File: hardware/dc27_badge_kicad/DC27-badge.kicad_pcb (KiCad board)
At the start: 4 copper layers, 79.1 x 184.5 mm, 129 parts, among them J101 Conn_ARM_JTAG_SWD_10, J102 ShittyAddOnL, J103 ShittyAddOnR, J104 Conn_02x20_Odd_Even, J501 SPK LEFT, J502 SPK_RIGHT, J601 USB_MICRO_RIGHT, SW101 UP, SW102 DN, SW103 LEFT, SW104 RIGHT, SW105 A, SW106 B, SW107 ENTER, SW108 RESET, SW401 POWER ON, U100 BMD-340-A-R-DC27-peripheral-c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, U301 IS31FL3216A, U401 MCP73831-2-OT, U402 LM1117-3.3, U403 MAX17055, U501 CS4344-CZZ, U502 LM4880, U601 CP2102N-A01-GQFN28, U602 TPD3E001DRLR, Y101 32.768Khz XTAL

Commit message: check in all of the gerbers and artwork
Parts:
- C506: footprint Capacitor_SMD:C_0603_1608Metric -> Capacitor_SMD:CP_Elec_5x5.3; moved to F.Cu
- U403: value MAX17055 -> MAX17055-10-TDFN-EP; footprint SON50P300X300X80-11N:SON50P300X300X80-11N -> tdfn-10-ep-2.00x2:tdfn-10-ep-2.00x2.50
- moved C506 23.4 mm to (118.3, 75.7), turned to 270 degrees
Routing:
- net Net-(C506-Pad1): track 2.39 -> 24.4 mm, vias 0 -> 1
- net Net-(C506-Pad2): track 10.0 -> 30.4 mm, vias 0 -> 1
- net I2C_SCK: track 332.5 -> 346.9 mm
- net Net-(C510-Pad1): track 62.1 -> 58.2 mm
- net BATT_CSN: track 453.5 -> 457.2 mm
- net Net-(C505-Pad1): track 48.4 -> 46.4 mm
- net BATT_CSP: track 15.6 -> 16.2 mm
- net I2S_SDOUT: track 88.8 -> 89.4 mm, vias 4 -> 3

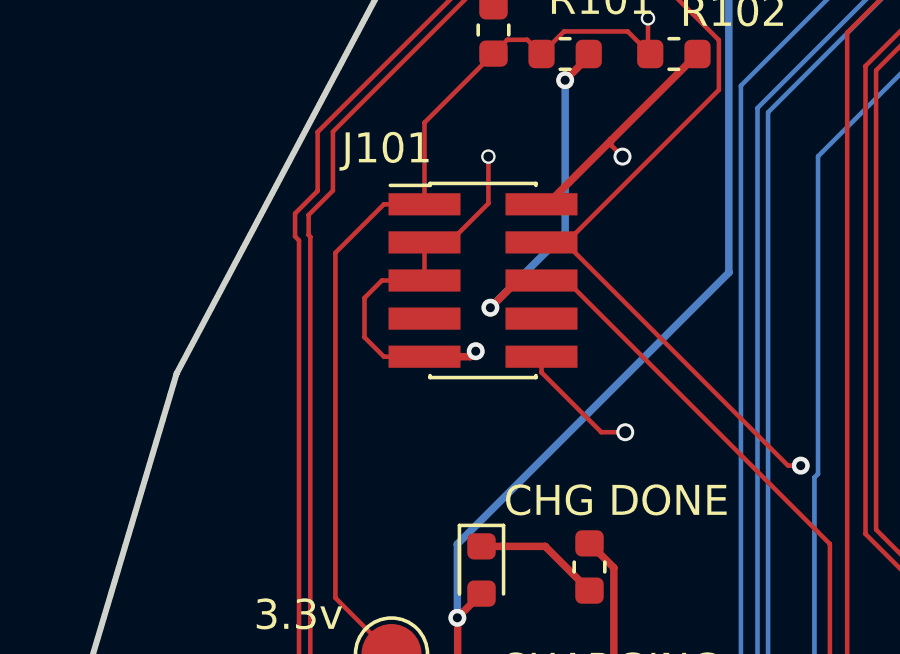
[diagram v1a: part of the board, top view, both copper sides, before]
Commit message: Closes issues #1, #2, #3 (see github)
  - #1 Removes copper fill under bmd340
  - #2 Add ON label
  - #3 Add pin 1 indicator and label for jtag
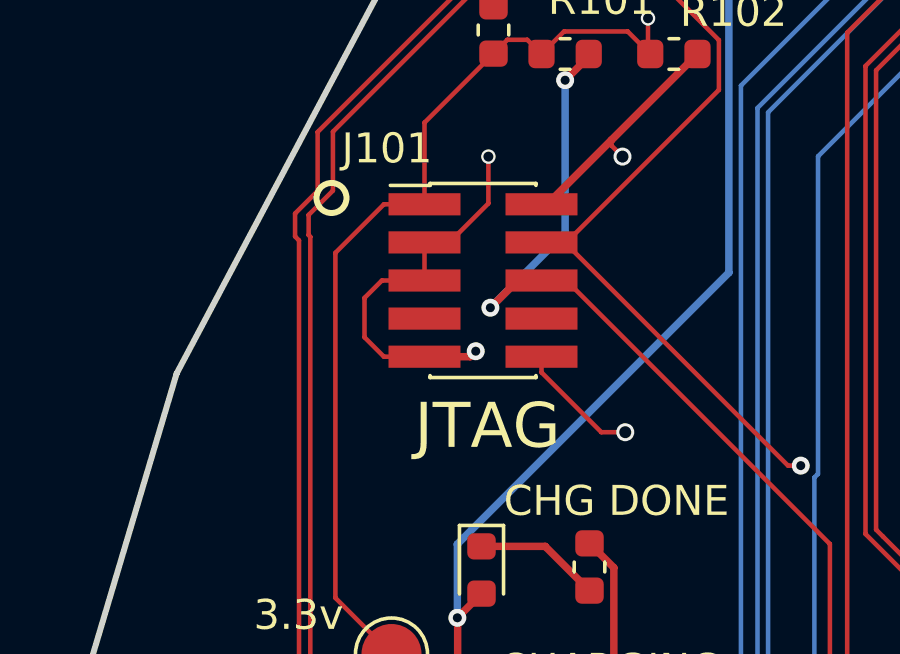
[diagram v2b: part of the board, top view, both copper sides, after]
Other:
- board text added: "JTAG"
- board text added: "ON"
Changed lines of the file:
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@@
-(kicad_pcb (version 20171130) (host pcbnew "(5.0.1-3-g963ef8bb5)")
+(kicad_pcb (version 20171130) (host pcbnew "(5.0.2-5)-5")
   (general
     (thickness 1.6)
-    (drawings 185)
+    (drawings 188)
     (tracks 2446)
     (zones 0)
@@
   )
   (setup
-    (last_trace_width 0.1524)
+    (last_trace_width 0.25)
     (user_trace_width 0.1524)
     (user_trace_width 0.254)
@@
       (net 156 BATT_CSN))
   )
+  (gr_text JTAG (at 81.6 107.6) (layer F.SilkS)
+    (effects (font (size 1.5 1.5) (thickness 0.3)))
+  )
+  (gr_circle (center 76.4 100) (end 76.7 100.4) (layer F.SilkS) (width 0.2))
+  (gr_text ON (at 71.2 115) (layer B.SilkS)
+    (effects (font (size 1.5 1.5) (thickness 0.3)) (justify mirror))
+  )
   (gr_text SDT_SPI_SCLK (at 119.2 140.2) (layer F.SilkS)
     (effects (font (size 1 1) (thickness 0.2)))
@@
     (connect_pads (clearance 0.508))
     (min_thickness 0.254)
-    (keepout (tracks not_allowed) (vias not_allowed) (copperpour allowed))
+    (keepout (tracks not_allowed) (vias not_allowed) (copperpour not_allowed))
     (fill (mode segment) (arc_segments 16) (thermal_gap 0.508) (thermal_bridge_width 0.508))
     (polygon

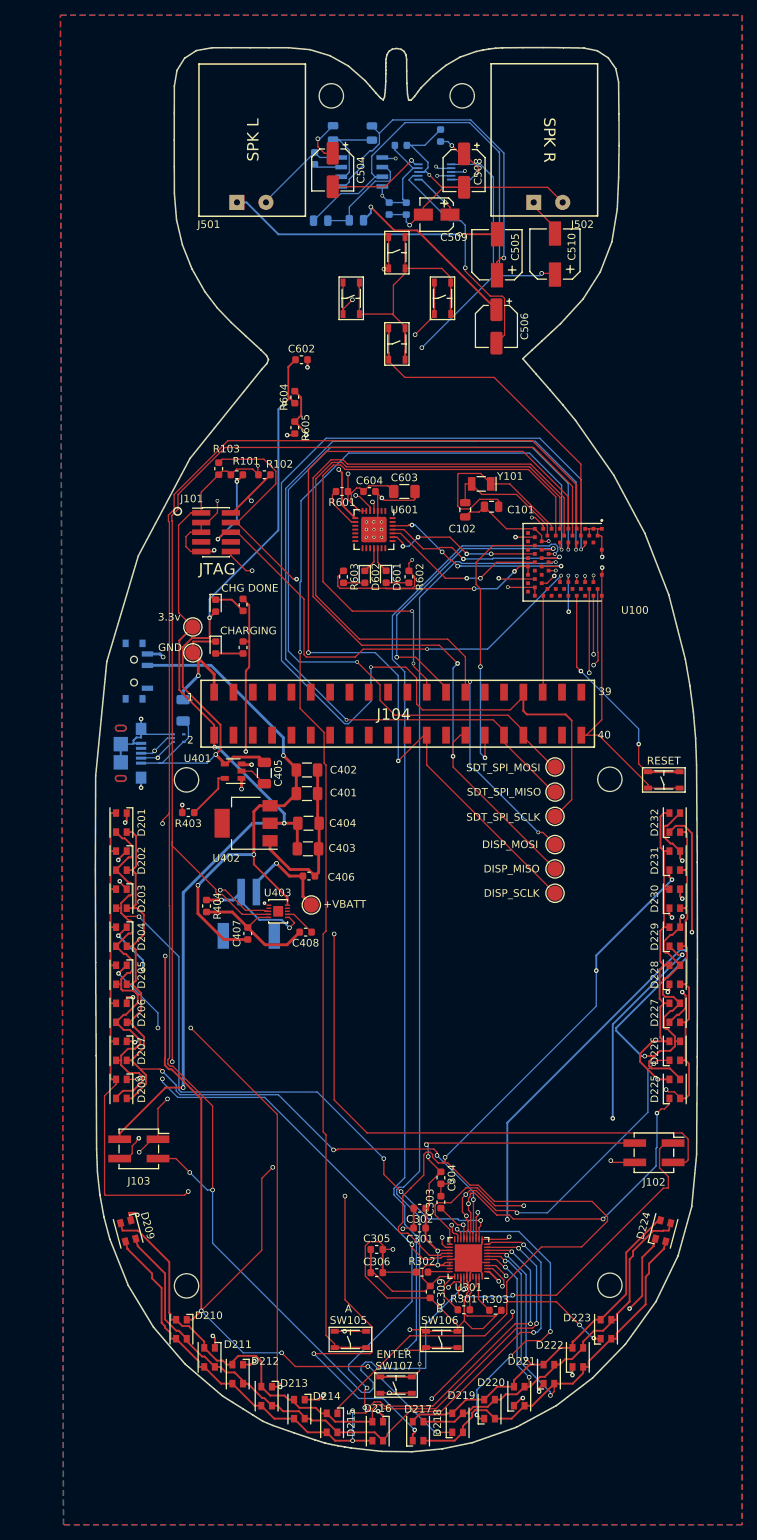
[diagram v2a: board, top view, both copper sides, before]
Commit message: add AST-01078 3d model and kicad footprint, check in current budget, update charging circut to MCP73833 instead of MCP73831:
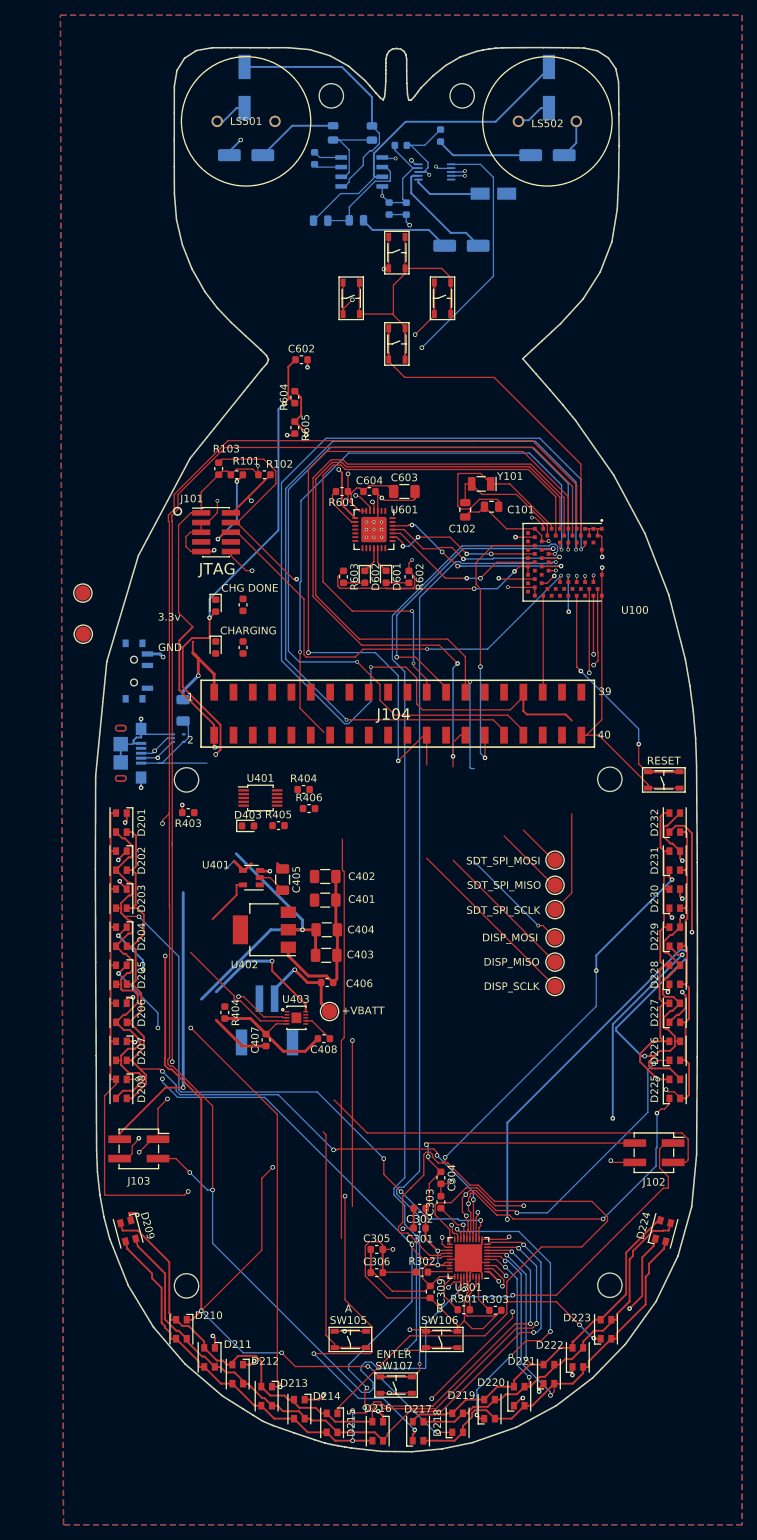
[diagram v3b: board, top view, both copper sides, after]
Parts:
- removed J501: SPK LEFT, Connector_Wire:SolderWirePad_1x02_P3.81mm_Drill0.8mm
- removed J502: SPK_RIGHT, Connector_Wire:SolderWirePad_1x02_P3.81mm_Drill0.8mm
- added D403: PWR GOOD, Diode_SMD:D_0603_1608Metric, F.Cu at (85.7, 141.3)
- added LS501: Speaker, lib_fp:AST-01708-MRR, F.Cu at (85.4, 48.8)
- added LS502: Speaker, lib_fp:AST-01708-MRR, F.Cu at (125.0, 48.8)
- added R404: 2.0k, Resistor_SMD:R_0603_1608Metric, F.Cu at (93.0, 136.6)
- added R405: 1K, Resistor_SMD:R_0603_1608Metric, F.Cu at (89.7, 141.3)
- added R406: 10K, Resistor_SMD:R_0603_1608Metric, F.Cu at (93.7, 139.1)
- added U401: MCP73833, Package_SO:MSOP-10_3x3mm_P0.5mm, F.Cu at (87.3, 137.7)
- C406: value 1uF -> 10uF
- C504, C505, C506, C508, C509, C510: moved to B.Cu
- D401: value CHG -> CHARGED
- D402: value DONE -> CHARGING (ORANGE)
- moved C505 39.8 mm to (85.2, 44.3)
- moved C510 21.9 mm to (125.2, 44.3)
- moved TP402 15.1 mm to (64.0, 110.8)
- moved TP403 14.6 mm to (64.0, 116.2)
- moved BT401 14.2 mm to (88.2, 166.9)
- moved C403 14.2 mm to (95.9, 158.4)
- moved C404 14.2 mm to (96.0, 155.0)
- moved C405 14.2 mm to (90.2, 148.4)
- moved C406 14.2 mm to (96.1, 161.9)
- moved C408 14.2 mm to (95.6, 169.3)
- moved TP401 14.2 mm to (96.4, 165.7)
- moved U403 14.2 mm to (92.0, 166.6)
- moved C401 14.2 mm to (95.8, 151.1)
- moved C402 14.2 mm to (95.8, 148.0)
- moved C407 14.2 mm to (88.0, 169.5)
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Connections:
- net NFC_ANT0 renamed Net-(U100-Pad25)
- net NFC_ANT1 renamed Net-(U100-Pad26)
- BT401 pad 2: BATT_CSP -> GND
- C101 pad 2: BATT_CSN -> GND
- C102 pad 2: BATT_CSN -> GND
- C301 pad 2: BATT_CSN -> GND
- C302 pad 2: BATT_CSN -> GND
- C303 pad 2: BATT_CSN -> GND
- C304 pad 2: BATT_CSN -> GND
- C305 pad 2: BATT_CSN -> GND
- C306 pad 2: BATT_CSN -> GND
- C309 pad 2: BATT_CSN -> GND
- C401 pad 1: VBATT -> Net-(C401-Pad1)
- C401 pad 2: BATT_CSN -> GND
- C402 pad 1: VBATT -> Net-(C401-Pad1)
- C402 pad 2: BATT_CSN -> GND
- C403 pad 2: BATT_CSN -> GND
- C404 pad 2: BATT_CSN -> GND
- C405 pad 2: BATT_CSN -> GND
- C406 pad 2: BATT_CSN -> GND
- C501 pad 2: BATT_CSN -> GND
- C502 pad 2: BATT_CSN -> GND
- C503 pad 2: BATT_CSN -> GND
- C507 pad 2: BATT_CSN -> GND
- C508 pad 2: BATT_CSN -> GND
- C509 pad 2: BATT_CSN -> GND
- C511 pad 2: BATT_CSN -> GND
- C601 pad 2: BATT_CSN -> GND
- C602 pad 2: BATT_CSN -> GND
- C603 pad 2: BATT_CSN -> GND
- C604 pad 2: BATT_CSN -> GND
- D402 pad 1: BATT_CSN -> Net-(D402-Pad1)
- D402 pad 2: Net-(D402-Pad2) -> VBUS
- J101 pad 3: BATT_CSN -> GND
- J101 pad 5: BATT_CSN -> GND
- J101 pad 9: BATT_CSN -> GND
- J102 pad 4: BATT_CSN -> GND
- J103 pad 4: BATT_CSN -> GND
- J104 pad 1: BATT_CSN -> GND
- J104 pad 40: BATT_CSN -> GND
- J601 pad 5: BATT_CSN -> GND
- J601 pad S1: BATT_CSN -> GND
- J601 pad S2: BATT_CSN -> GND
- J601 pad S3: BATT_CSN -> GND
- J601 pad S4: BATT_CSN -> GND
- J601 pad S5: BATT_CSN -> GND
- J601 pad S6: BATT_CSN -> GND
- R302 pad 1: BATT_CSN -> GND
- R303 pad 2: BATT_CSN -> GND
- R401 pad 1: Net-(R401-Pad1) -> Net-(D401-Pad1)
- R401 pad 2: Net-(D401-Pad1) -> Net-(R401-Pad2)
- R402 pad 1: Net-(R401-Pad1) -> Net-(D402-Pad1)
- R402 pad 2: Net-(D402-Pad2) -> Net-(R402-Pad2)
- R403 pad 2: BATT_CSN -> GND
- R605 pad 2: BATT_CSN -> GND
- SW101 pad P$1: BATT_CSN -> GND
- SW101 pad P$2: BATT_CSN -> GND
- SW102 pad P$1: BATT_CSN -> GND
- SW102 pad P$2: BATT_CSN -> GND
- SW103 pad P$1: BATT_CSN -> GND
- SW103 pad P$2: BATT_CSN -> GND
- SW104 pad P$1: BATT_CSN -> GND
- SW104 pad P$2: BATT_CSN -> GND
- SW105 pad P$1: BATT_CSN -> GND
- SW105 pad P$2: BATT_CSN -> GND
- SW106 pad P$1: BATT_CSN -> GND
- SW106 pad P$2: BATT_CSN -> GND
- SW107 pad P$3: BATT_CSN -> GND
- SW107 pad P$4: BATT_CSN -> GND
- SW108 pad P$3: BATT_CSN -> GND
- SW108 pad P$4: BATT_CSN -> GND
- SW401 pad 2: VBATT -> Net-(C401-Pad1)
- TP403 pad 1: BATT_CSN -> GND
- U100 pad 1: BATT_CSN -> GND
- U100 pad 16: BATT_CSN -> GND
- U100 pad 18: BATT_CSN -> GND
- U100 pad 2: BATT_CSN -> GND
- U100 pad 29: BATT_CSN -> GND
- U100 pad 3: BATT_CSN -> GND
- U100 pad 30: BATT_CSN -> GND
- U100 pad 4: BATT_CSN -> GND
- U100 pad 45: BATT_CSN -> GND
- U100 pad 46: BATT_CSN -> GND
- U100 pad 47: BATT_CSN -> GND
- U100 pad 5: BATT_CSN -> GND
- U100 pad 55: BATT_CSN -> GND
- U301 pad 11: BATT_CSN -> GND
- U301 pad 26: BATT_CSN -> GND
- U301 pad 35: BATT_CSN -> GND
- U301 pad 36: BATT_CSN -> GND
- U301 pad 4: BATT_CSN -> GND
- U301 pad 40: BATT_CSN -> GND
- U301 pad 41: BATT_CSN -> GND
- U401 pad 2: BATT_CSN -> GND
- U402 pad 1: BATT_CSN -> GND
- U402 pad 3: VBATT -> Net-(C401-Pad1)
- U501 pad 8: BATT_CSN -> GND
- U502 pad 4: BATT_CSN -> GND
- U601 pad 29: BATT_CSN -> GND
- U601 pad 3: BATT_CSN -> GND
- U602 pad 3: BATT_CSN -> GND
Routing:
- net BATT_CSN: track 457.2 -> 18.0 mm, vias 25 -> 0
- net GND: track 0.00 -> 402.5 mm, vias 0 -> 25
- net CS3: track 240.8 -> 173.9 mm
- net VBATT: track 71.6 -> 25.4 mm, vias 3 -> 1
- net Net-(C505-Pad2): track 36.3 -> 4.63 mm, vias 1 -> 0
- net Net-(R401-Pad1): track 28.2 -> 0.23 mm, vias 2 -> 0
- net BATT_CSP: track 16.2 -> 0.22 mm, vias 2 -> 0
- net Net-(C506-Pad2): track 30.4 -> 15.0 mm, vias 1 -> 0
- net Net-(C504-Pad2): track 12.9 -> 27.7 mm, vias 1 -> 2
- net Net-(C510-Pad1): track 58.2 -> 43.5 mm, vias 1 -> 0
- net Net-(C505-Pad1): track 46.4 -> 32.9 mm, vias 1 -> 0
- net Net-(C506-Pad1): track 24.4 -> 12.0 mm, vias 1 -> 0
- net Net-(C504-Pad1): track 6.06 -> 10.6 mm, vias 1 -> 0
- net Net-(D401-Pad1): track 4.21 -> 0.00 mm
- net Net-(D402-Pad2): track 3.60 -> 0.00 mm
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- added copper zone on B.Cu, net GND
- added copper zone on F.Cu, net GND
- added copper zone on GND, net GND
- removed copper zone on B.Cu, net BATT_CSN
- removed copper zone on F.Cu, net BATT_CSN
- removed copper zone on GND, net BATT_CSN
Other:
- board text removed: "SPK L"
- board text removed: "SPK R"

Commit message: add in the new buttons and joystick interrupts, make new schematic for joypads, update the pcb (not done)
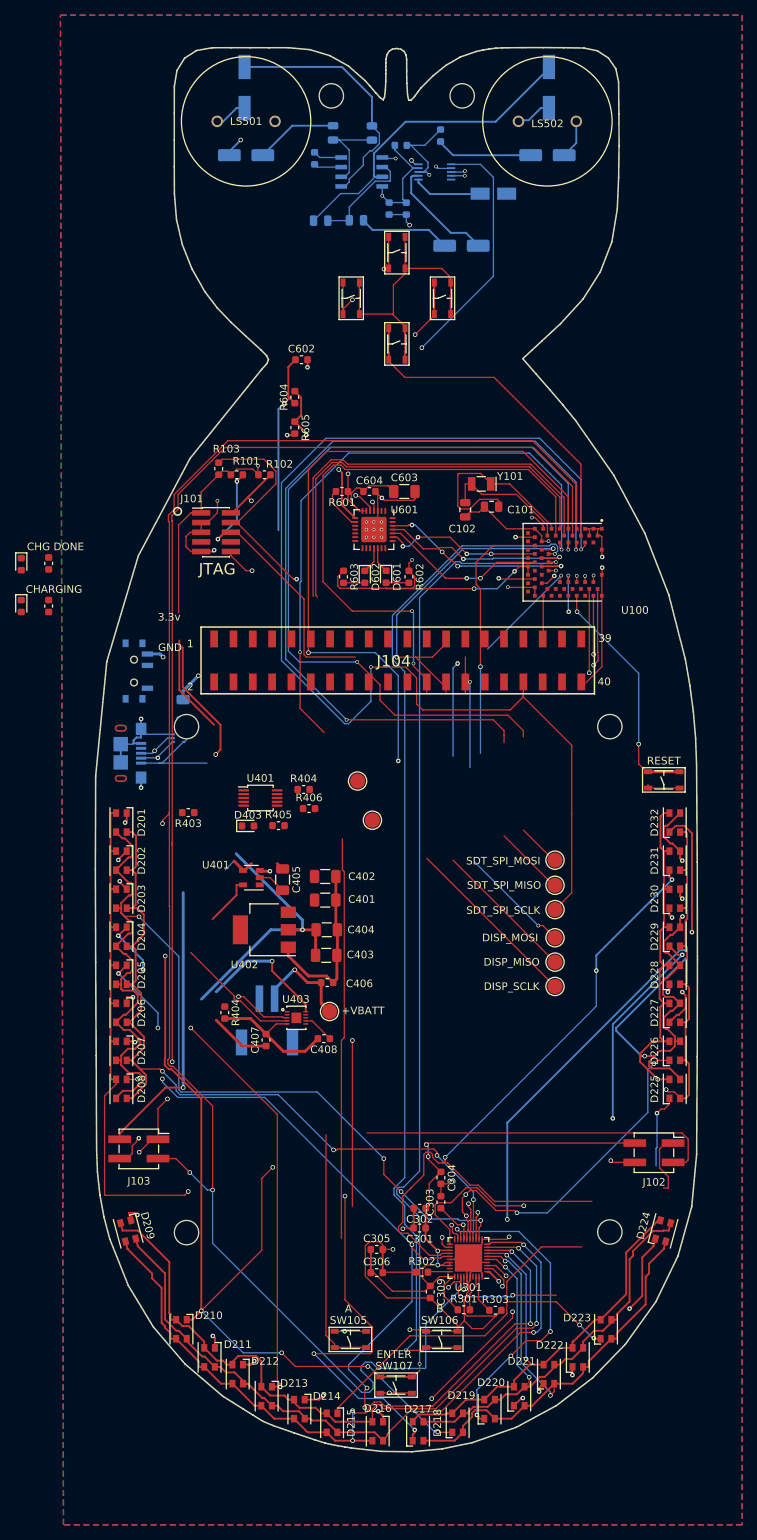
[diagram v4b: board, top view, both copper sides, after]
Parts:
- moved TP402 48.4 mm to (102.0, 140.6)
- moved TP403 40.9 mm to (100.0, 135.4)
- moved D401 26.1 mm to (55.9, 107.0)
- moved D402 26.1 mm to (55.9, 112.5)
- moved R401 26.1 mm to (59.5, 106.8)
- moved R402 26.1 mm to (59.5, 112.5)
- moved J104 7.00 mm to (105.3, 119.6)
- moved MH701 7.00 mm to (77.6, 128.3)
- moved MH703 7.00 mm to (77.6, 194.7)
- moved MH704 7.00 mm to (133.2, 194.7)
- moved MH702 6.92 mm to (133.2, 128.3)
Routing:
- net DISP_MOSI: track 110.3 -> 69.4 mm, vias 2 -> 1
- net VBUS: track 86.6 -> 46.9 mm, vias 3 -> 1
- net CS6: track 194.1 -> 157.1 mm
- net I2C_SDA: track 263.6 -> 230.7 mm
- net GND: track 402.5 -> 371.5 mm, vias 25 -> 24
- net CS1: track 219.5 -> 189.4 mm, vias 8 -> 7
- net ~RESET_TGTMCU: track 84.1 -> 54.1 mm
- net CS4: track 212.5 -> 189.1 mm
- net DEBUG_SWO: track 71.7 -> 53.9 mm, vias 4 -> 3
- net Net-(J104-Pad3): track 0.00 -> 16.7 mm, vias 0 -> 1
- net CS3: track 173.9 -> 157.5 mm
- net DISP_MISO: track 115.9 -> 105.6 mm
- net DISP_SCLK: track 123.7 -> 114.0 mm
- net SDT_SPI_SCK: track 148.4 -> 157.0 mm
- net AVCC: track 400.6 -> 392.1 mm, vias 15 -> 14
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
